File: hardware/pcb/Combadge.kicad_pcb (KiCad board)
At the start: 2 copper layers, 33.7 x 31 mm, 33 parts, among them J1 Conn_01x02_Female, J2 Conn_01x02_Female, J3 TOUCH, J4 USB_B_Micro, SW1 CSS-1210TB, U1 ESP32-WROOM-32, U2 MAX98357, U3 MCP73831-2-OT, U4 RN4989, U5 NCP160AMX330TBG

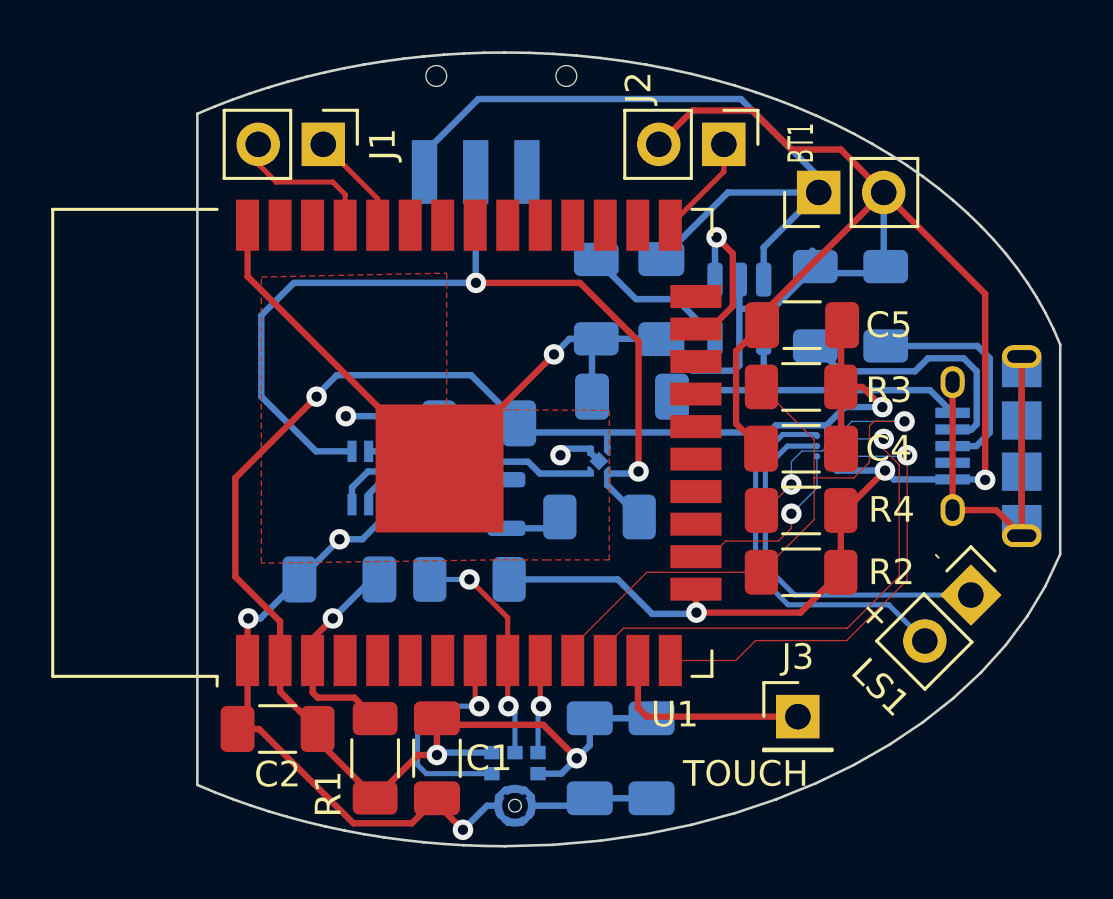
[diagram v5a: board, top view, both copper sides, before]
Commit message: Add indicator LED
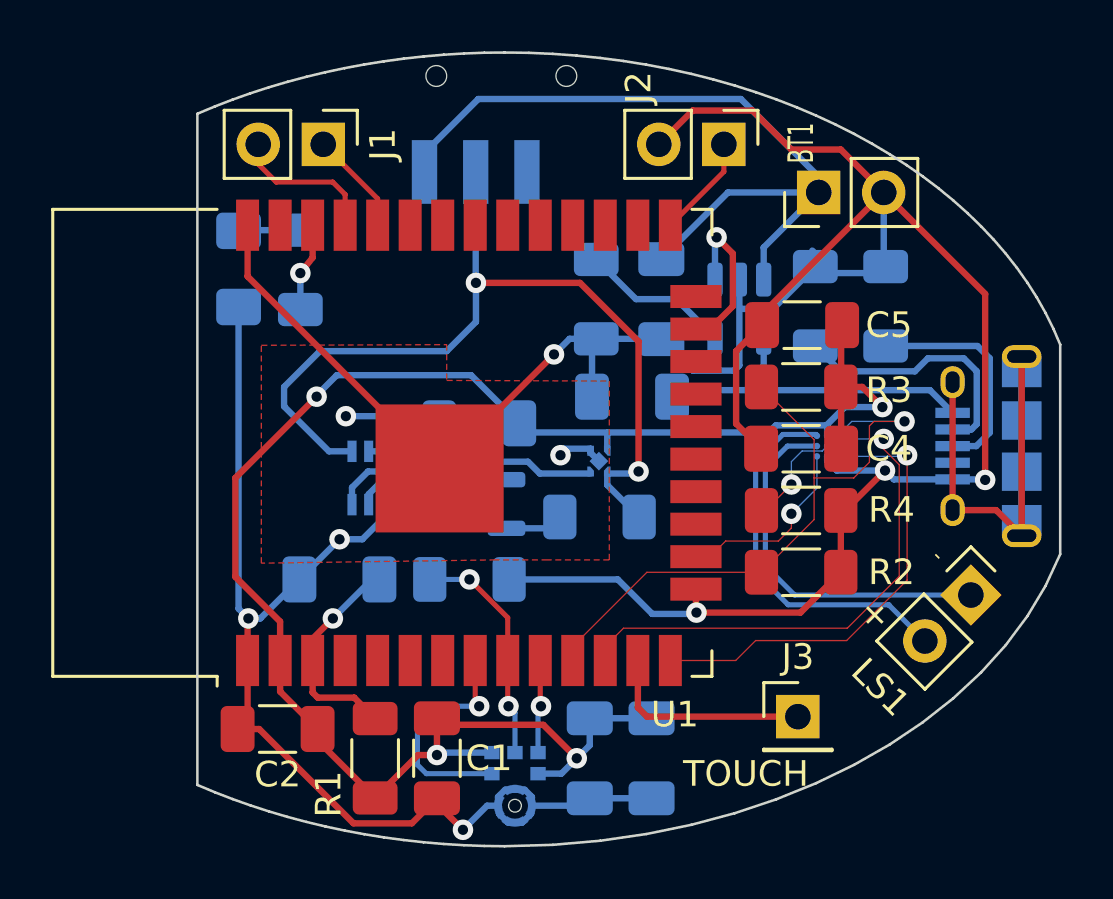
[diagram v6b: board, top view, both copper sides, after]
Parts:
- added D2: LED, LED_SMD:LED_1206_3216Metric_Pad1.42x1.75mm_HandSolder, B.Cu at (145.5, 88.7)
- added R10: 100, Resistor_SMD:R_1206_3216Metric_Pad1.30x1.75mm_HandSolder, B.Cu at (148.0, 88.8)
- U2: value MAX98357 -> MAX98357AEWL+T
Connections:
- U1 pad 36: unconnected-(U1-IO22-Pad36) -> Net-(U1-IO22)
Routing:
- net GND: track 146.1 -> 158.4 mm
- net Net-(U1-IO22): track 0.00 -> 3.59 mm, vias 0 -> 1
- net /INDICATOR: track 0.00 -> 2.42 mm
- net Net-(U4-EMITTER2): track 36.7 -> 34.4 mm

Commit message: Replace zener diode setup with TLV431
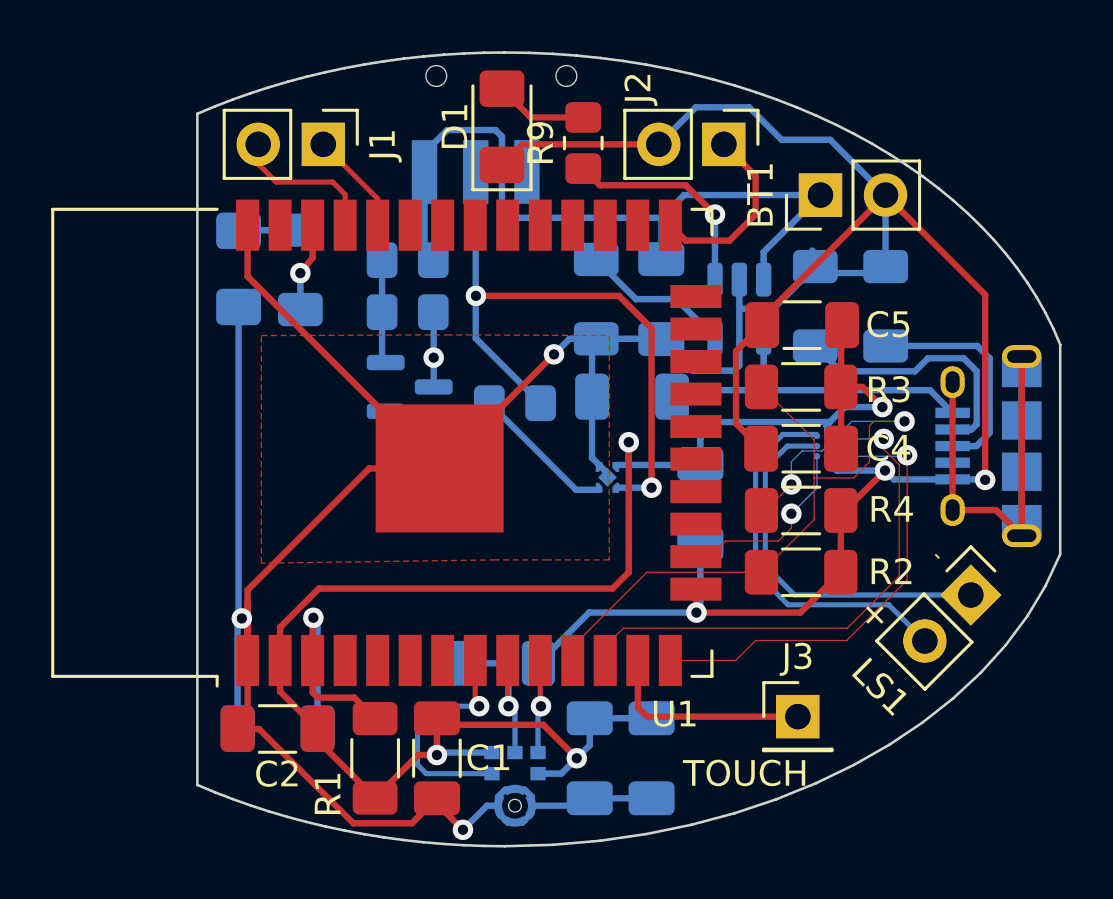
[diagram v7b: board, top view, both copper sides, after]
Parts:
- added R11: 10k, Resistor_SMD:R_0805_2012Metric_Pad1.20x1.40mm_HandSolder, B.Cu at (156.3, 94.0)
- added R12: 220k, Resistor_SMD:R_0805_2012Metric_Pad1.20x1.40mm_HandSolder, B.Cu at (152.1, 88.4)
- added R13: 120k, Resistor_SMD:R_0805_2012Metric_Pad1.20x1.40mm_HandSolder, B.Cu at (152.1, 90.4)
- D1: value D_Zener_Dual_CommonAnode_KKA -> LED; footprint Package_TO_SOT_SMD:SOT-23 -> LED_SMD:LED_1206_3216Metric_Pad1.42x1.75mm_HandSolder; moved to F.Cu
- R9: value 10 -> 150; footprint Resistor_SMD:R_1206_3216Metric_Pad1.30x1.75mm_HandSolder -> Resistor_SMD:R_0805_2012Metric_Pad1.20x1.40mm_HandSolder; moved to F.Cu
- U4: value RN4989 -> TL431DBZ; footprint RN4989:RN4989 -> Package_TO_SOT_SMD:SOT-23
- moved D1 14.8 mm to (155.8, 83.2), turned to 90 degrees
- moved R9 14.6 mm to (159.0, 83.8), turned to 90 degrees
- moved C10 9.19 mm to (163.6, 97.9), turned to -90 degrees
- moved C3 6.30 mm to (147.1, 106.7)
- moved U4 3.90 mm to (152.2, 93.3), turned to 0 degrees
- moved R5 3.47 mm to (155.7, 104.1)
- moved U5 0.72 mm to (159.9, 96.9)
- moved BT1 0.12 mm to (168.3, 85.9)
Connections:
- net Net-(D1-K-Pad2) renamed /Power/CHRG_FULL
- D1 pad 1: unconnected-(D1-K-Pad1) -> GND
- R9 pad 1: Net-(U4-EMITTER2) -> Net-(U3-STAT)
- SW1 pad 2: Net-(U4-EMITTER2) -> Net-(U5-VIN)
- U1 pad 23: /Power/CHRG_STATUS -> unconnected-(U1-IO15-Pad23)
- U3 pad 1: /Power/CHRG_STATUS -> Net-(U3-STAT)
- U4 pad 1: GND -> Net-(U4-K)
- U4 pad 2: Net-(D1-A) -> Net-(U4-REF)
- U4 pad 3: Net-(U4-COLLECTOR2) -> GND
- U5 pad 3: Net-(U4-COLLECTOR2) -> Net-(U4-K)
- U5 pad 4: Net-(U4-EMITTER2) -> Net-(U5-VIN)
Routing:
- net Net-(U4-EMITTER2): track 34.4 -> 0.00 mm, vias 2 -> 0
- net Net-(U5-VIN): track 0.00 -> 25.1 mm, vias 0 -> 2
- net GND: track 158.4 -> 176.9 mm, vias 9 -> 7
- net Net-(U4-COLLECTOR2): track 10.6 -> 0.00 mm
- net Net-(U4-K): track 0.00 -> 9.87 mm
- net Net-(U3-STAT): track 0.00 -> 8.43 mm, vias 0 -> 1
- net /Power/CHRG_STATUS: track 6.44 -> 0.00 mm, vias 1 -> 0
- net Net-(D1-A): track 4.39 -> 0.00 mm
- net Net-(U4-REF): track 0.00 -> 4.26 mm
- net /ESP_BOOT: track 4.02 -> 7.26 mm
- net +3.3V: track 69.6 -> 66.9 mm
- net /MIC_DATA: track 9.05 -> 7.10 mm, vias 2 -> 1
- net Net-(U1-EN): track 8.53 -> 10.2 mm
- net /Power/CHRG_FULL: track 2.27 -> 3.64 mm
- net +BATT: track 30.4 -> 29.4 mm
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
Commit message: Make all resistors 1206 and LEDs 0805
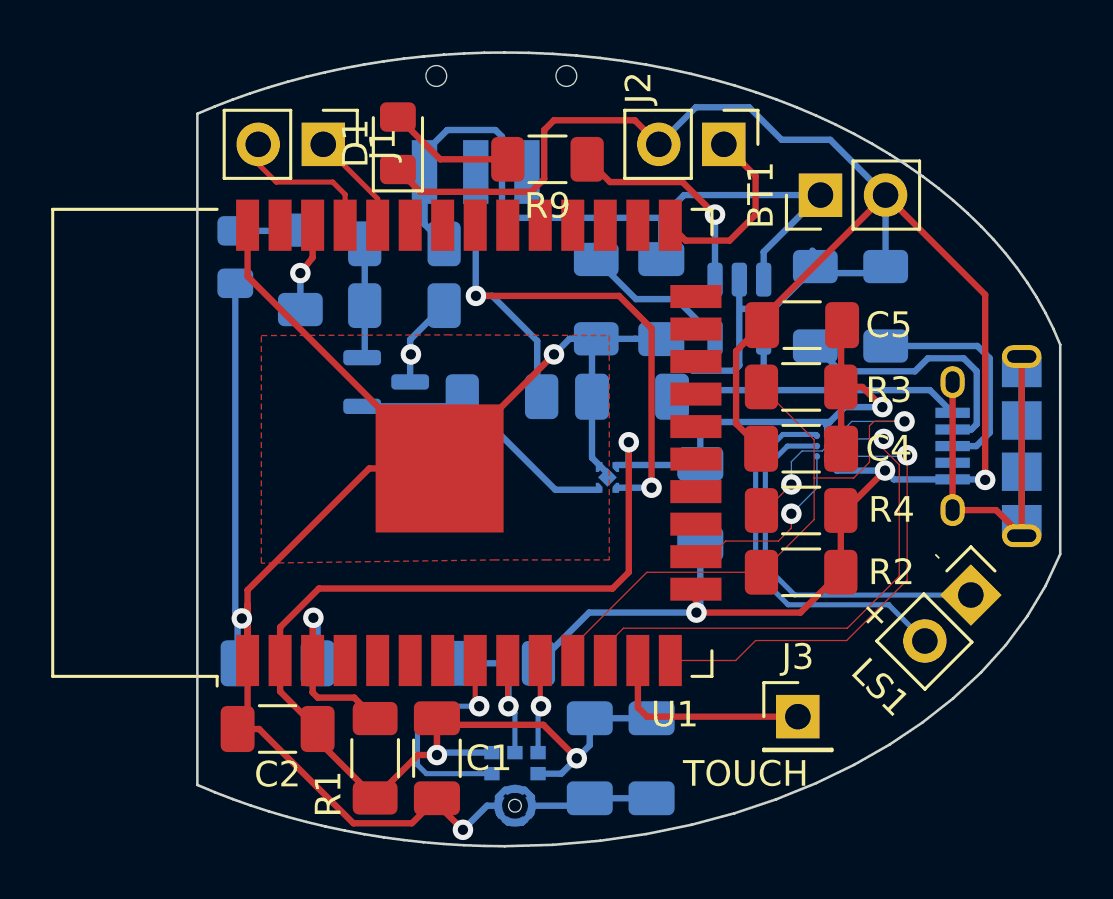
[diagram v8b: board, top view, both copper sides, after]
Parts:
- D1, D2: footprint LED_SMD:LED_1206_3216Metric_Pad1.42x1.75mm_HandSolder -> LED_SMD:LED_0805_2012Metric_Pad1.15x1.40mm_HandSolder
- R11, R12, R13, R9: footprint Resistor_SMD:R_0805_2012Metric_Pad1.20x1.40mm_HandSolder -> Resistor_SMD:R_1206_3216Metric_Pad1.30x1.75mm_HandSolder
- moved D1 4.11 mm to (151.8, 83.8)
- moved C3 2.54 mm to (147.1, 104.1)
- moved R9 1.53 mm to (157.6, 84.5), turned to 180 degrees
- moved U4 0.94 mm to (151.3, 93.2)
- moved R12 0.65 mm to (152.0, 87.8)
- moved R11 0.57 mm to (155.8, 93.7)
- moved D2 0.48 mm to (145.4, 88.3)
- moved R13 0.28 mm to (152.0, 90.2)
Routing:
- net GND: track 176.9 -> 182.6 mm
- net Net-(U1-EN): track 10.2 -> 7.64 mm
- net /Power/CHRG_FULL: track 3.64 -> 4.98 mm
- net Net-(U4-K): track 9.87 -> 10.9 mm
